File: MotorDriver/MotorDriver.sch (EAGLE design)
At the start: 26 parts, among them U1 MCP4013, U2 DRV8848, U3 ATTINY841

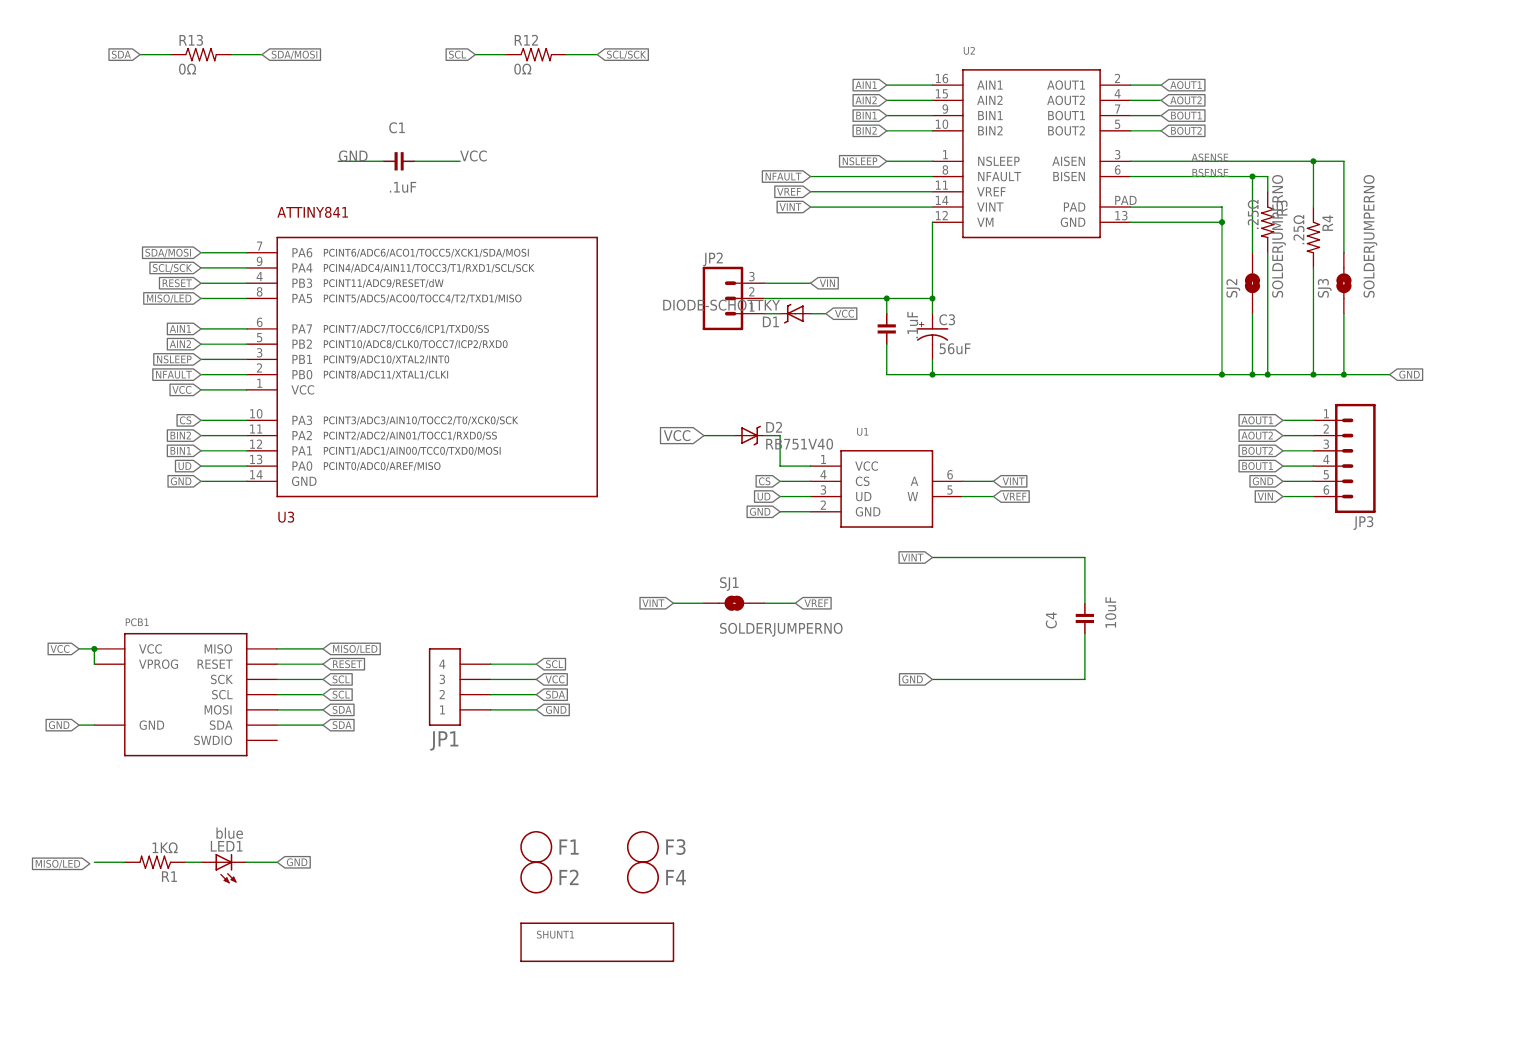
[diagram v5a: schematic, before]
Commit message: Added unique board prefixes to part numbers due to CM requirements
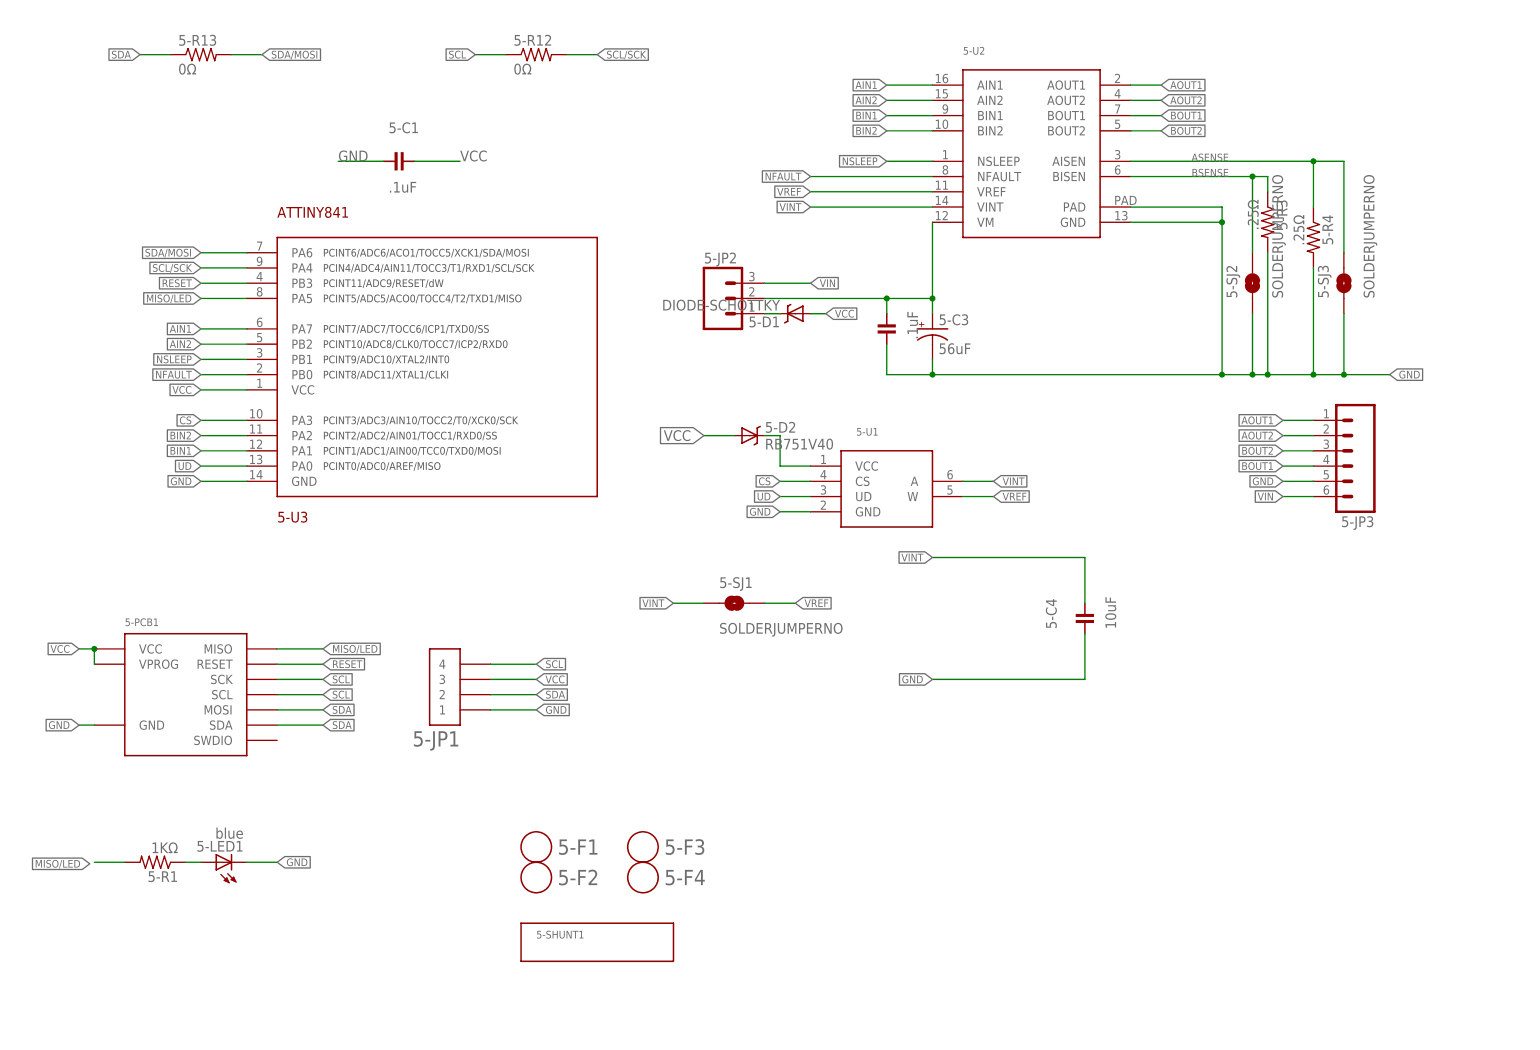
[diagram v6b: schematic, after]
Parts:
- renumbered C1 to 5-C1, C2 to 5-C2, C3 to 5-C3, C4 to 5-C4, D1 to 5-D1, D2 to 5-D2, F1 to 5-F1, F2 to 5-F2, F3 to 5-F3, F4 to 5-F4, JP1 to 5-JP1, JP2 to 5-JP2, JP3 to 5-JP3, LED1 to 5-LED1, PCB1 to 5-PCB1, R1 to 5-R1, R12 to 5-R12, R13 to 5-R13, R3 to 5-R3, R4 to 5-R4, SJ1 to 5-SJ1, SJ2 to 5-SJ2, SJ3 to 5-SJ3, U1 to 5-U1, U2 to 5-U2, U3 to 5-U3
